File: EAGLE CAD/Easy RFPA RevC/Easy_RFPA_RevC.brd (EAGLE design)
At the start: 127 x 147.3 mm, 286 parts, among them IC1 LM741D, IC2 LM741D, IC3 LM393D, IC5 74AHC1G00DBV, IC6 74LS74D, IC7 74AHC1G86DBV, J401 HDR_2X1282836-1282836-1, J402 KK_PCFAN, Q1 IRF630, Q101 IRF520N, Q102 IRF630, Q2 MOSFET_NBSS123SOT23, Q201 IRF630, Q202 IRF630, Q3 NPNMMBT3904SOT23_BEC, Q301 MOSFET_NBSS123SOT23, Q302 PNPSOT23_BEC, Q303 NPNMMBT3904SOT23_BEC, Q4 PNPSOT23_BEC, SW1 SPST_NO_TACT_RA43125608371643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, SW2 SPST_NO_TACT_RA43125608371643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, T1 HP1_TRAFO, T102 HP4_TRAFO, U1 OPAMP_QUADTLV274IDSOIC14, U302 OPAMP_QUADTLV274IDSOIC14, U401 LDO_3TERMMC78M12CTGTO220_VERT, U402 LDO_3TERMMC78M05CTGTO220_VERT, X1 1-227161-0, X2 1-227161-0, X4 1-227161-0, X402 HEATSINK_OMNI_DUALOMNI-UNI-30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

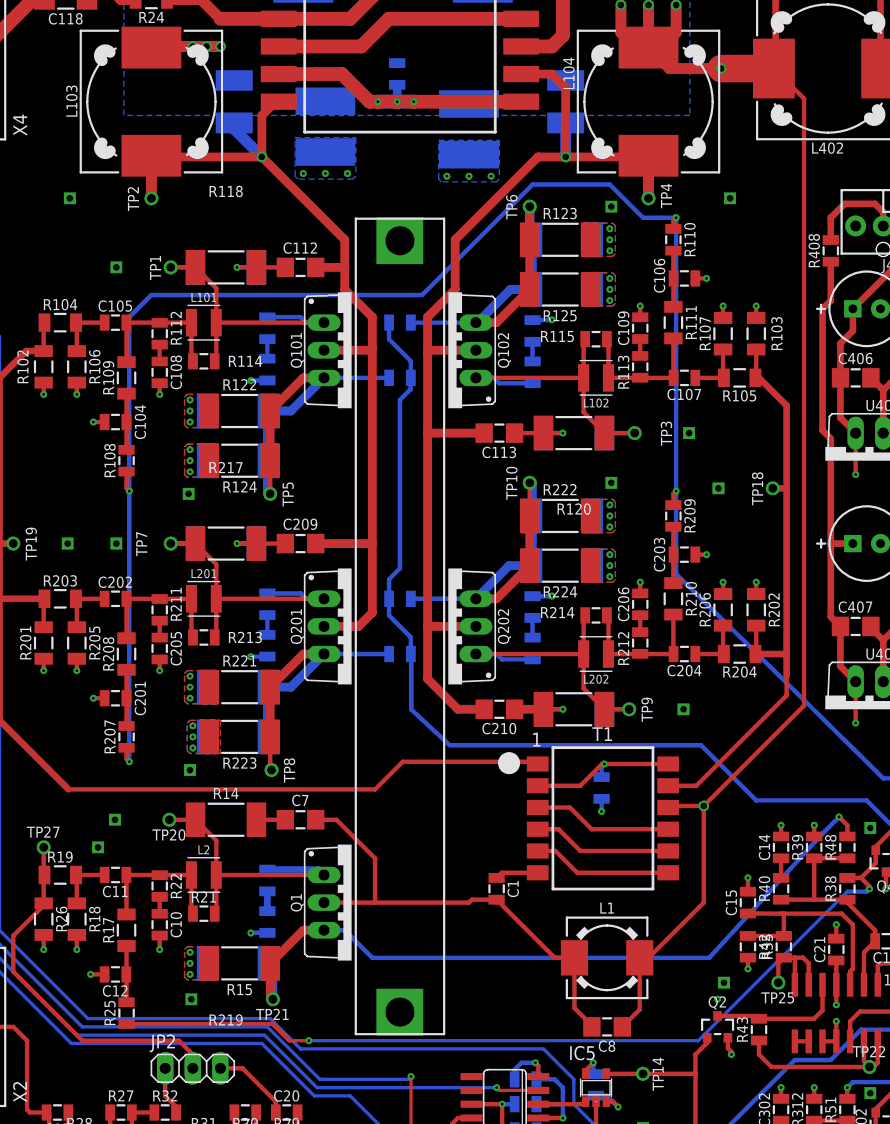
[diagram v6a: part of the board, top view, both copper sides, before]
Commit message: Add bypass cap for VB near S2 bias Add 40mm wide heatsink to library adjust some trace widths
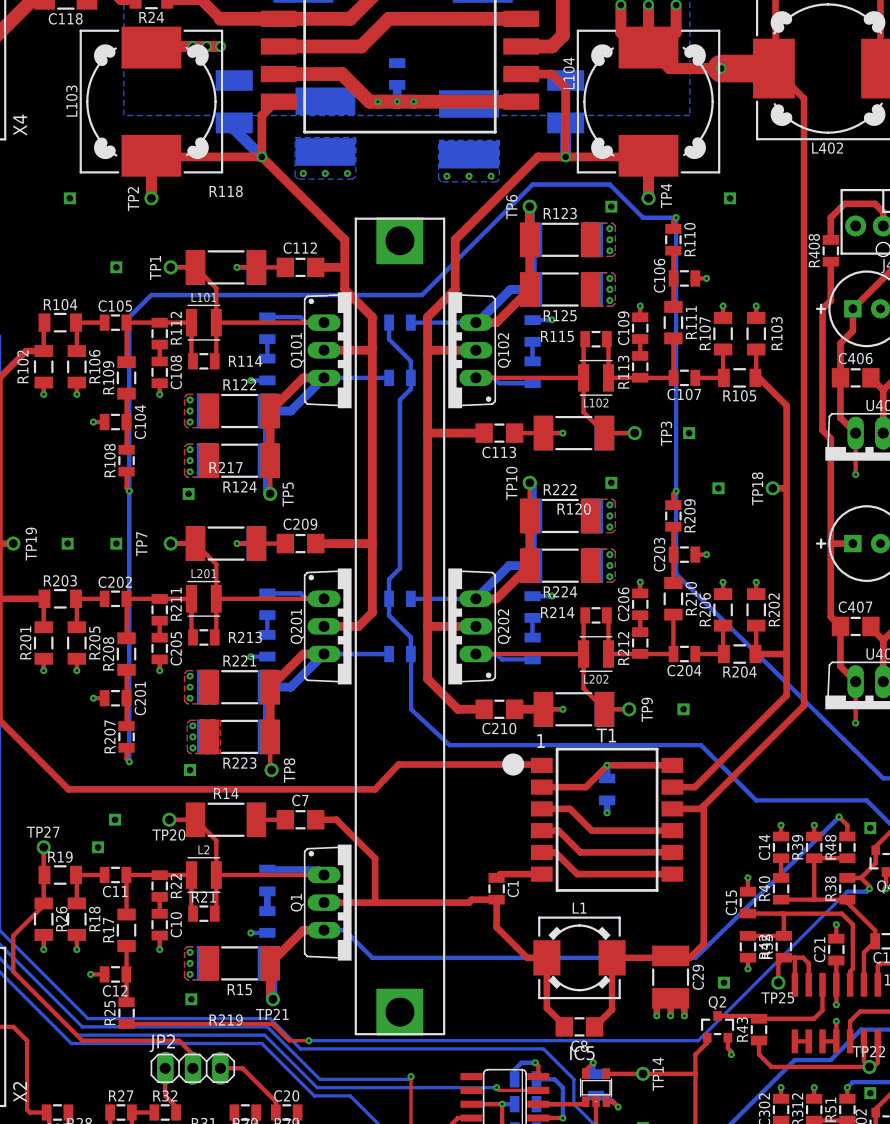
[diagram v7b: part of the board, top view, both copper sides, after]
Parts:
- added C29: DNP, MDT_C:C1812
- moved C8 2.54 mm to (67.3, 33.0)
- moved L1 2.54 mm to (67.3, 39.4)
- moved R101 0.52 mm to (69.8, 54.9)
- moved T1 0.40 mm to (69.8, 52.1)
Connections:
- net GND: now also C29.2
- net VB: now also C29.1
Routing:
- net GND: track 141.7 -> 148.7 mm, vias 151 -> 153
- net VB: track 149.6 -> 154.2 mm, vias 8 -> 7
- net S2_DP: track 43.6 -> 42.3 mm

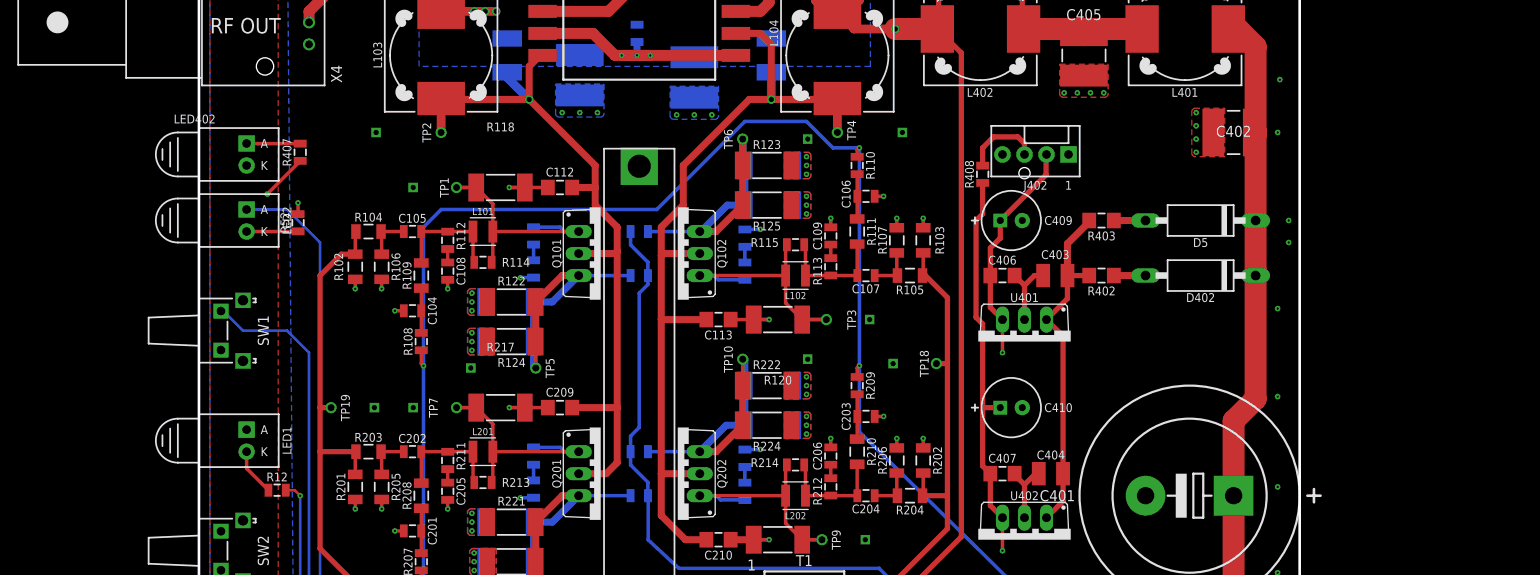
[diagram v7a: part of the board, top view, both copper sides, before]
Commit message: 24V regulator
Add discrete 24V linear regulator in schematic
Using one of my TO220 FETs for the pass device for now
Added TL431 to VREF library
Also added two more mounting holes to board
And the footprint for a clip-on TO-220 heatsink
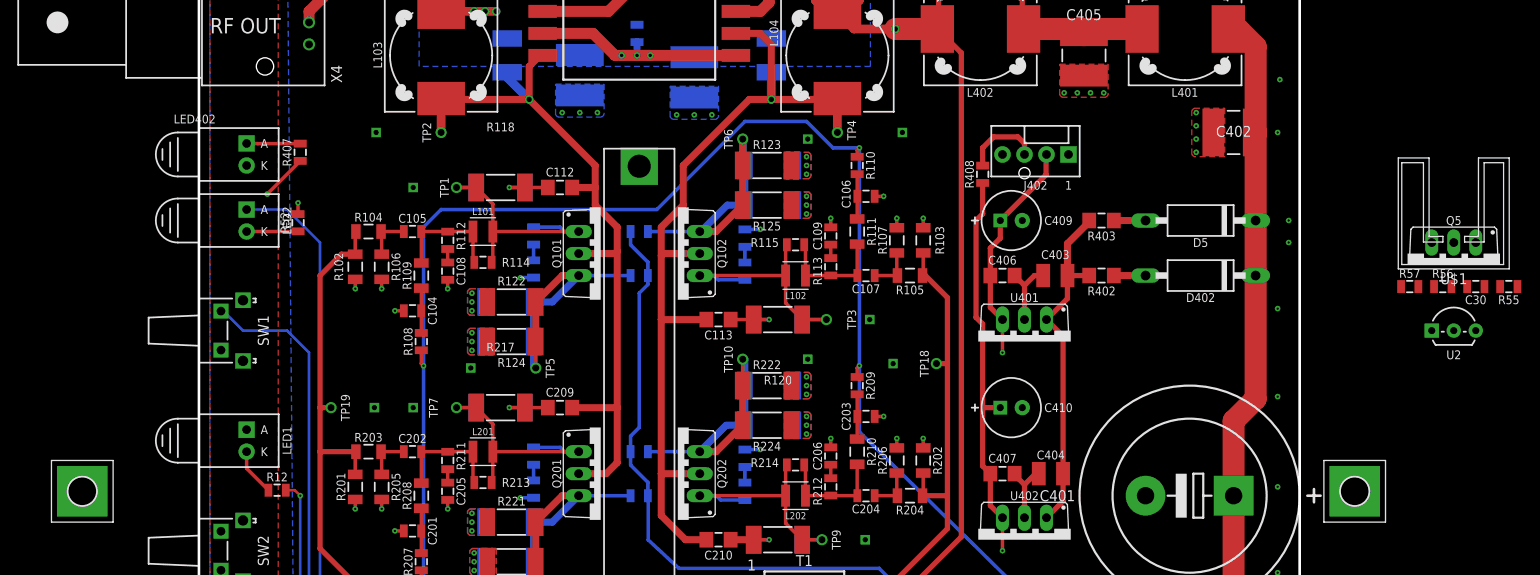
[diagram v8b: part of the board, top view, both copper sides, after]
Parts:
- added C30: 33pF, MDT_C:0805_IPC-7351B
- added H1, H2: MOUNT-PAD-SQUARE3.2, holes:3,2-PAD-SQUARE
- added Q5: IRF630, MDT_TRANS:TO220BV
- added R55, R56, R57: 590, MDT_R:0805_IPC-7351B
- added U$1: (no value), MDT_HEATSINK:ATS-PCBT1085
- added U2: ADJ_ZENERTL431AILPRAGTO-92-LPRE, MDT_VREF:TO-92-FORMED
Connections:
- net N$44 renamed VB_FUSED
- net N$45 renamed VB_CONN
- removed net N$43: C403.1, C404.1, R402.2, R403.2, U401.1, U402.1
- removed net N$46: C401.+, C402.1, D402.C, D5.C, L401.1, R401.2
- new net N$91: C30.2, R56.1, R57.2, U2.1
- new net N$92: C30.1, Q5.G, R55.2, U2.3
- new net VB_ICL: C401.+, C402.1, D402.C, D5.C, L401.1, Q5.D, R401.2, R55.1
- net +24V: now also C403.1, C404.1, Q5.S, R402.2, R403.2, R57.1, U401.1, U402.1
- net GND: now also R56.2, U2.2
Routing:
- net VB_ICL: track 0.00 -> 79.0 mm
- net N$46: track 79.0 -> 0.00 mm
- net N$43: track 40.6 -> 0.00 mm
- net +24V: track 23.9 -> 64.6 mm
